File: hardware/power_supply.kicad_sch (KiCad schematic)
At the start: 0 parts

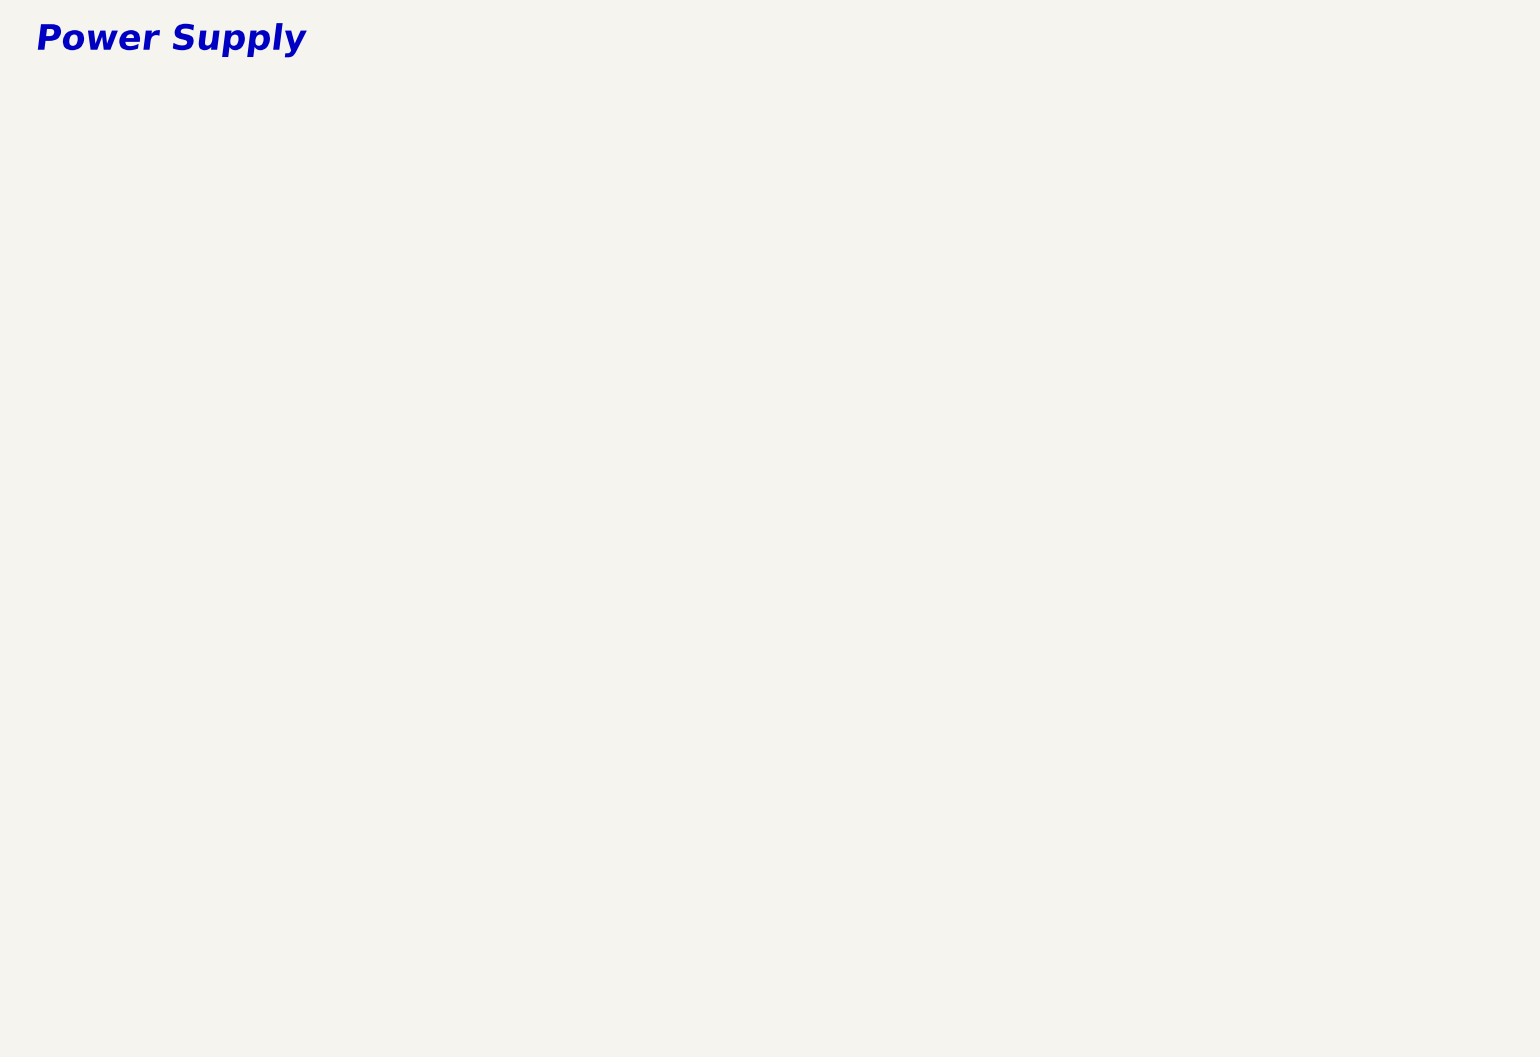
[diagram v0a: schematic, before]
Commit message: schematic and BOM done
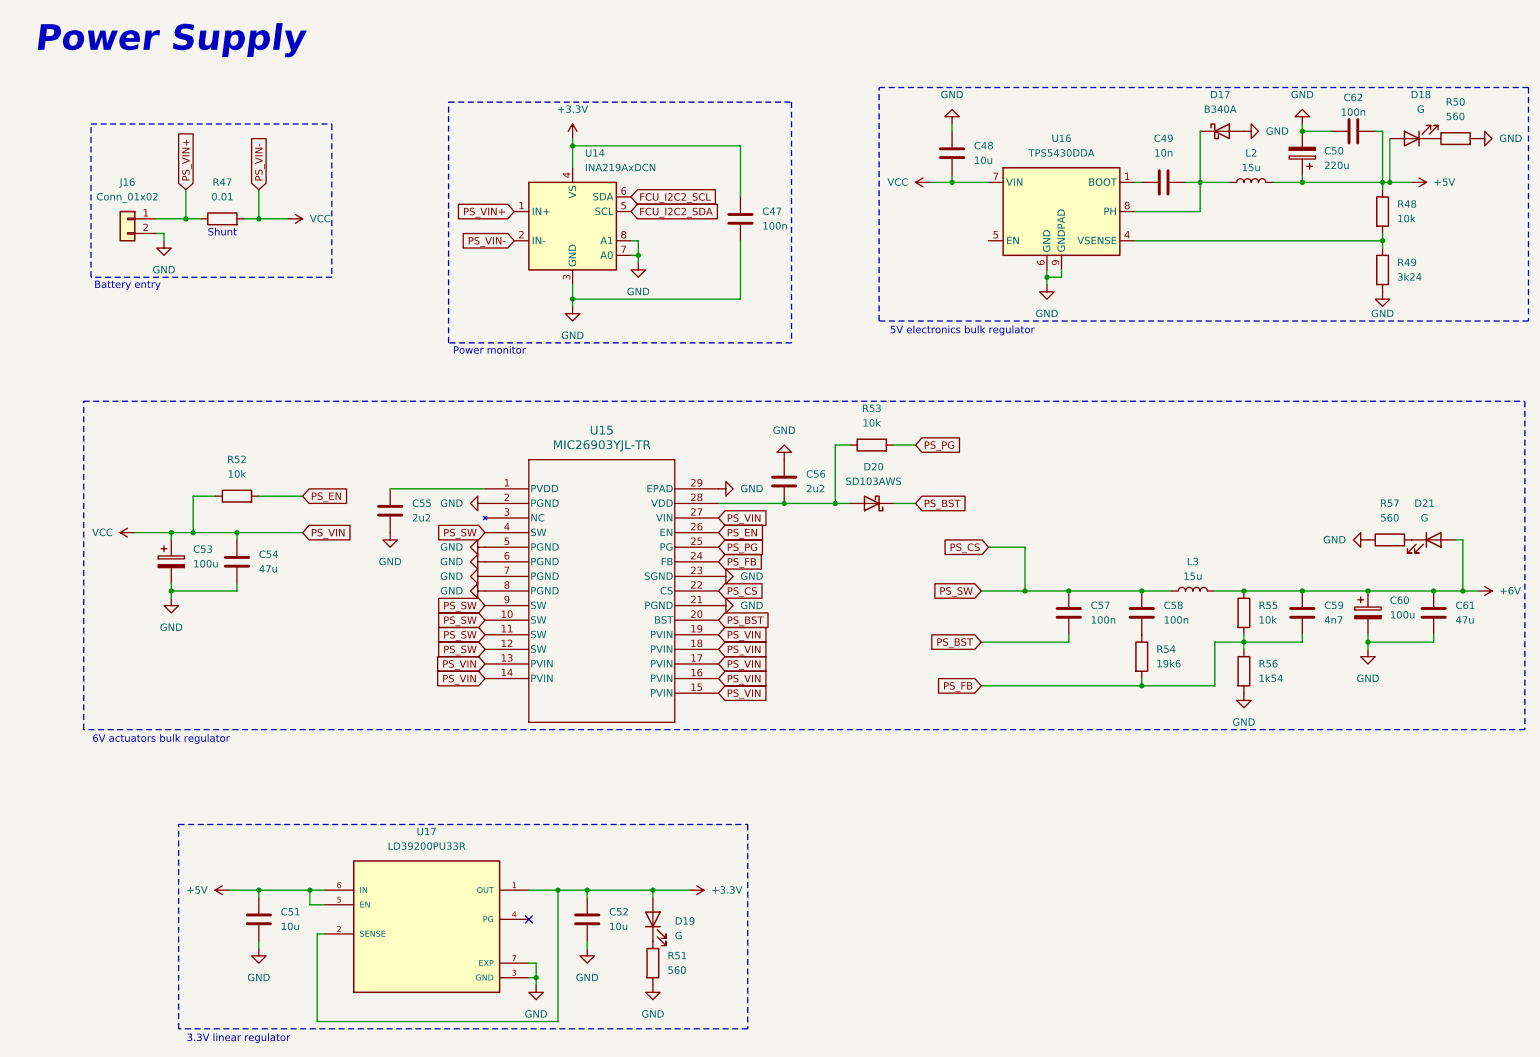
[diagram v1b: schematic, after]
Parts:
- added C47, C57, C58, C62: 100n, Capacitor_SMD:C_0603_1608Metric, symbol Device:C
- added C48, C51, C52: 10u, Capacitor_SMD:C_1206_3216Metric, symbol Device:C
- added C49: 10n, Capacitor_SMD:C_0603_1608Metric, symbol Device:C
- added C50: 220u, Capacitor_SMD:CP_Elec_8x10, symbol Device:C_Polarized
- added C53, C60: 100u, Capacitor_SMD:CP_Elec_8x10, symbol Device:C_Polarized
- added C54, C61: 47u, Capacitor_SMD:C_1206_3216Metric, symbol Device:C
- added C55, C56: 2u2, Capacitor_SMD:C_0603_1608Metric, symbol Device:C
- added C59: 4n7, Capacitor_SMD:C_0603_1608Metric, symbol Device:C
- added D17: B340A, airplane:DIOM5226X240N, symbol Device:D_Schottky
- added D18, D19, D21: G, LED_SMD:LED_0603_1608Metric, symbol Device:LED
- added D20: SD103AWS, airplane:SOD2713X115N, symbol Device:D_Schottky
- added J16: Conn_01x02, Connector_AMASS:AMASS_XT60-M_1x02_P7.20mm_Vertical, symbol Connector_Generic:Conn_01x02
- added L2: 15u, Inductor_SMD:L_APV_APH0615, symbol Device:L
- added L3: 15u, Inductor_SMD:L_APV_APH1030, symbol Device:L
- added R47: 0.01, Resistor_SMD:R_2512_6332Metric, symbol Device:R
- added R48, R52, R53, R55: 10k, Resistor_SMD:R_0603_1608Metric, symbol Device:R
- added R49: 3k24, Resistor_SMD:R_0603_1608Metric, symbol Device:R
- added R50, R51, R57: 560, Resistor_SMD:R_0603_1608Metric, symbol Device:R
- added R54: 19k6, Resistor_SMD:R_0603_1608Metric, symbol Device:R
- added R56: 1k54, Resistor_SMD:R_0603_1608Metric, symbol Device:R
- added U14: INA219AxDCN, Package_TO_SOT_SMD:SOT-23-8, symbol Sensor_Energy:INA219AxDCN
- added U15: MIC26903YJL-TR, airplane:CONV_MIC28510YJL-TR, symbol components:MIC26903YJL-TR
- added U16: TPS5430DDA, Package_SO:TI_SO-PowerPAD-8_ThermalVias, symbol Regulator_Switching:TPS5430DDA
- added U17: LD39200PU33R, airplane:SON95P300X300X100-7N, symbol components:LD39200PU33R
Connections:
- new net: C55.1, U15.1 (PVDD)
- new net: R48.2, R49.1, U16.4 (VSENSE)
- new net: C56.2, D20.2 (A), R53.1, U15.28 (VDD)
- new net: D21.1 (K), R57.2
- new net: C49.1, U16.1 (BOOT)
- new net: C49.2, D17.1 (K), L2.1, U16.8 (PH)
- new net: D18.1 (K), R50.1
- new net: C58.2, R54.1
- new net: D19.1 (K), R51.1
- new net +3.3V: C47.1, C52.1, D19.2 (A), U14.4 (VS), U17.1 (OUT), U17.2 (SENSE)
- new net +5V: C50.1, C51.1, C62.1, D18.2 (A), L2.2, R48.1, U17.5 (EN), U17.6 (IN)
- new net +6V: C59.1, C60.1, C61.1, D21.2 (A), L3.2, R55.1
- new net FCU_I2C2_SCL: U14.6 (SDA)
- new net FCU_I2C2_SDA: U14.5 (SCL)
- new net GND: C47.2, C48.1, C50.2, C51.2, C52.2, C53.2, C54.2, C55.2, C56.1, C60.2, C61.2, C62.2, D17.2 (A), J16.2 (Pin_2), R49.2, R50.2, R51.2, R56.2, R57.1, U14.3 (GND), U14.7 (A0), U14.8 (A1), U15.2 (PGND), U15.21 (PGND), U15.23 (SGND), U15.29 (EPAD), U15.5 (PGND), U15.6 (PGND), U15.7 (PGND), U15.8 (PGND), U16.6 (GND), U16.9 (GNDPAD), U17.3 (GND), U17.7 (EXP)
- new net PS_BST: C57.2, D20.1 (K), U15.20 (BST)
- new net PS_CS: C57.1, C58.1, L3.1, U15.10 (SW), U15.11 (SW), U15.12 (SW), U15.22 (CS), U15.4 (SW), U15.9 (SW)
- new net PS_EN: R52.2, U15.26 (EN)
- new net PS_FB: C59.2, R54.2, R55.2, R56.1, U15.24 (FB)
- new net PS_PG: R53.2, U15.25 (PG)
- new net PS_VIN+: J16.1 (Pin_1), R47.1, U14.1 (IN+)
- new net VCC: C48.2, C53.1, C54.1, R47.2, R52.1, U14.2 (IN-), U15.13 (PVIN), U15.14 (PVIN), U15.15 (PVIN), U15.16 (PVIN), U15.17 (PVIN), U15.18 (PVIN), U15.19 (PVIN), U15.27 (VIN), U16.7 (VIN)
- no-connect marks 0 -> 1
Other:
- note added: "3.3V linear regulator"
- note added: "5V electronics bulk regulator"
- note added: "6V actuators bulk regulator"
- note added: "Battery entry"
- note added: "Power monitor"
- note added: "Shunt"
